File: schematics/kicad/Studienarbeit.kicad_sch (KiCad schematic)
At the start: 41 parts, among them J1 Barrel_Jack_Switch, U1 ESP32-WROOM-32E, U2 PCM5102, U3 MCP6001-OT, U4 MCP6001-OT, U5 MCP6001, U6 TPA711

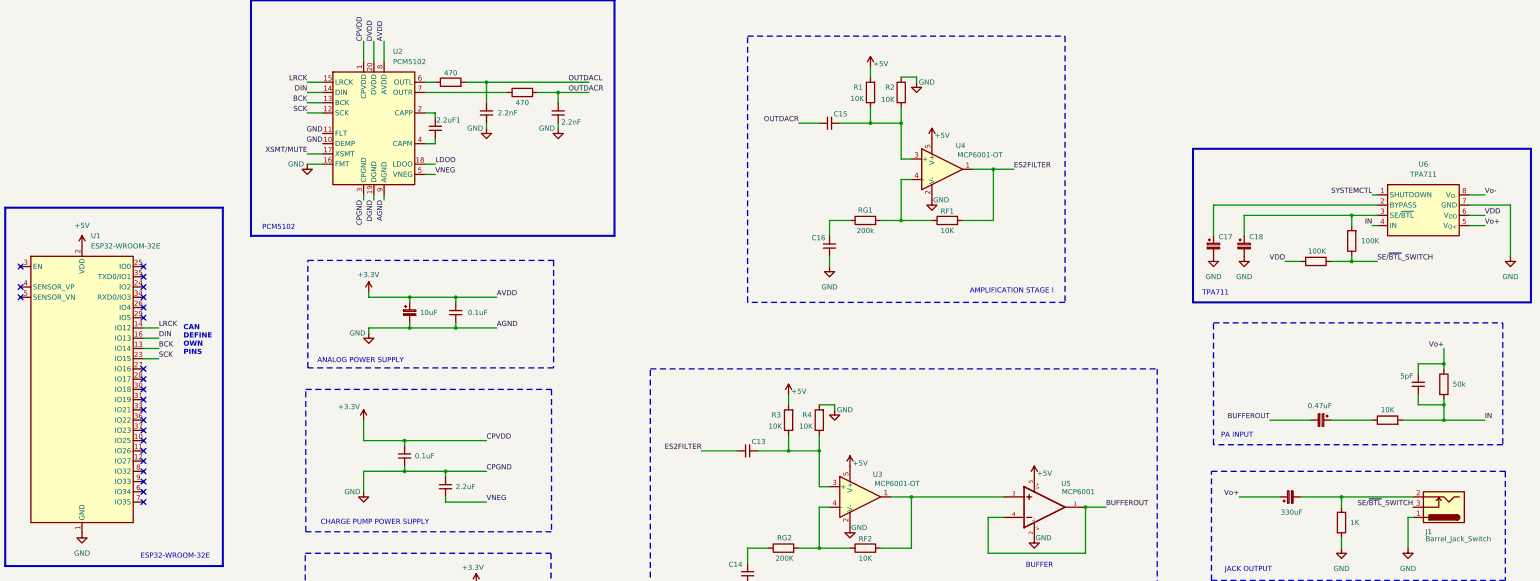
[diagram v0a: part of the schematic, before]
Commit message: KiCad: Fixed a few ERC errors.
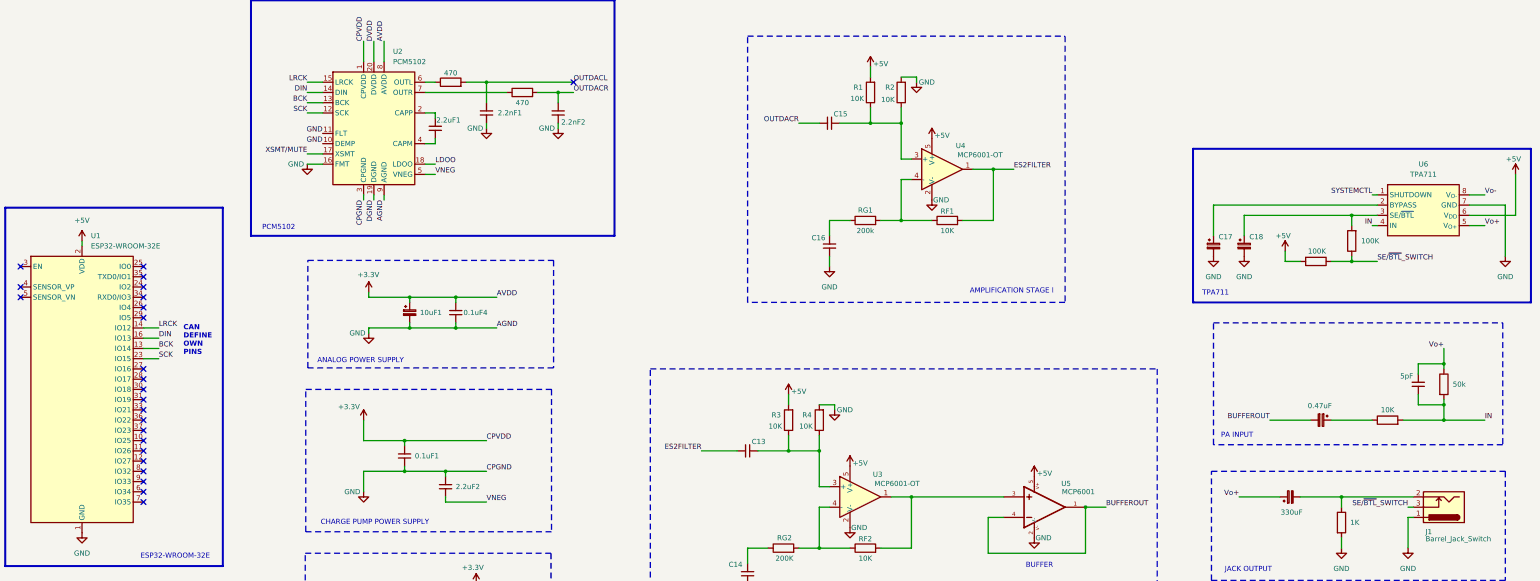
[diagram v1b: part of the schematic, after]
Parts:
- renumbered 0.1uF to 0.1uF1, 0.1uF to 0.1uF4, 10uF to 10uF1, 2.2nF to 2.2nF1, 2.2nF to 2.2nF2, 2.2uF to 2.2uF2, ROUTDACL to ROUTDACL1, ROUTDACR to ROUTDACR1
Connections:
- net VDD is gone; now on net +5V: R12.2, U6.6 (V_{DD})
- no-connect marks 23 -> 24

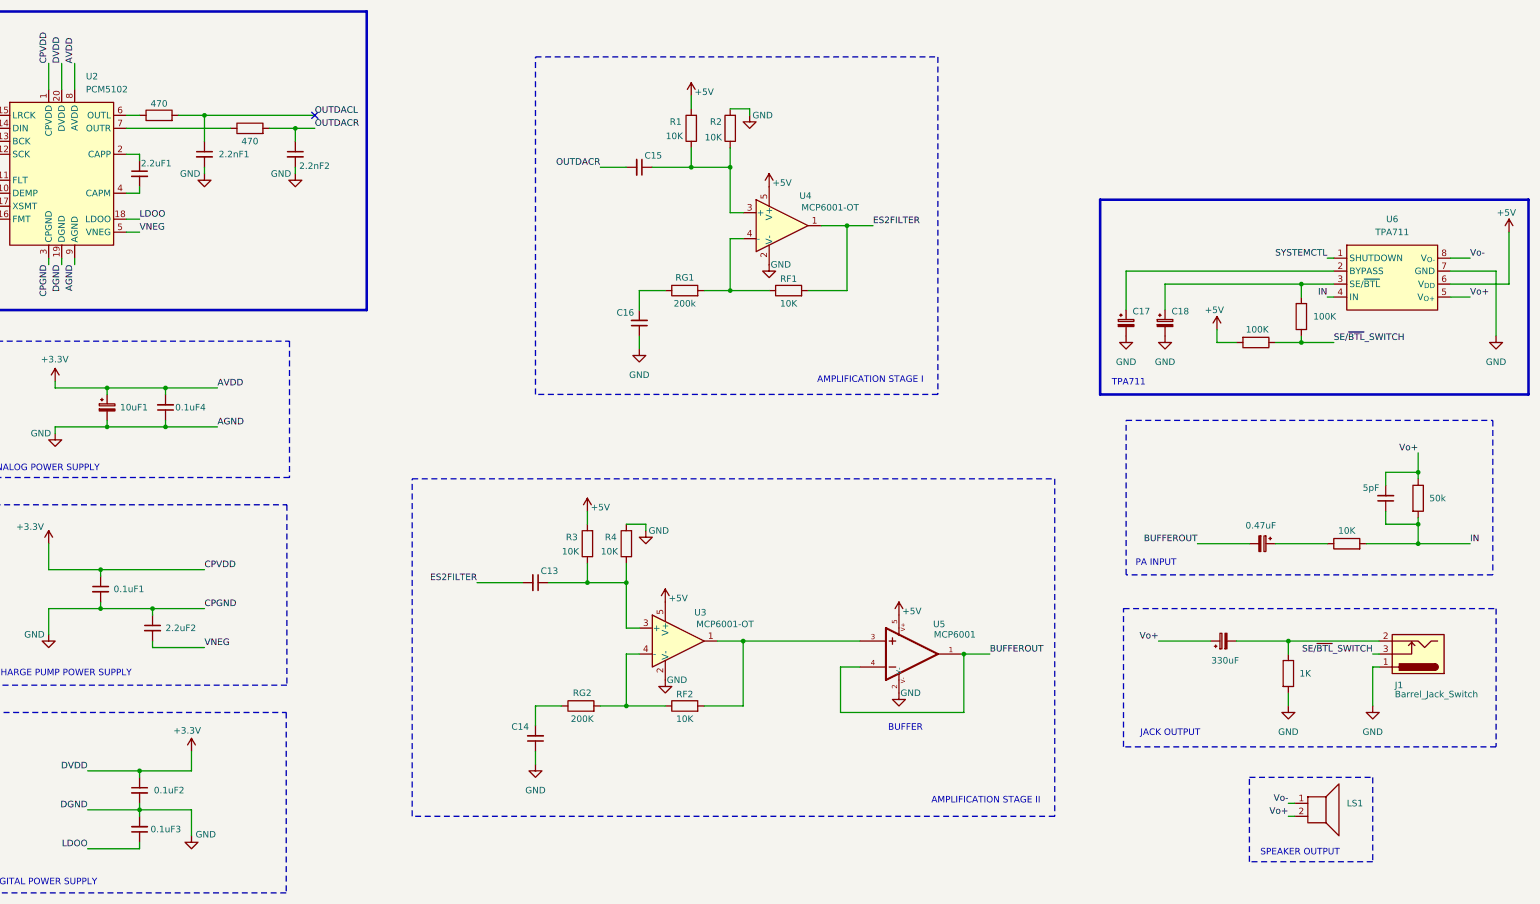
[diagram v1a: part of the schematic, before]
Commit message: KiCad: Dimentioned Cs.
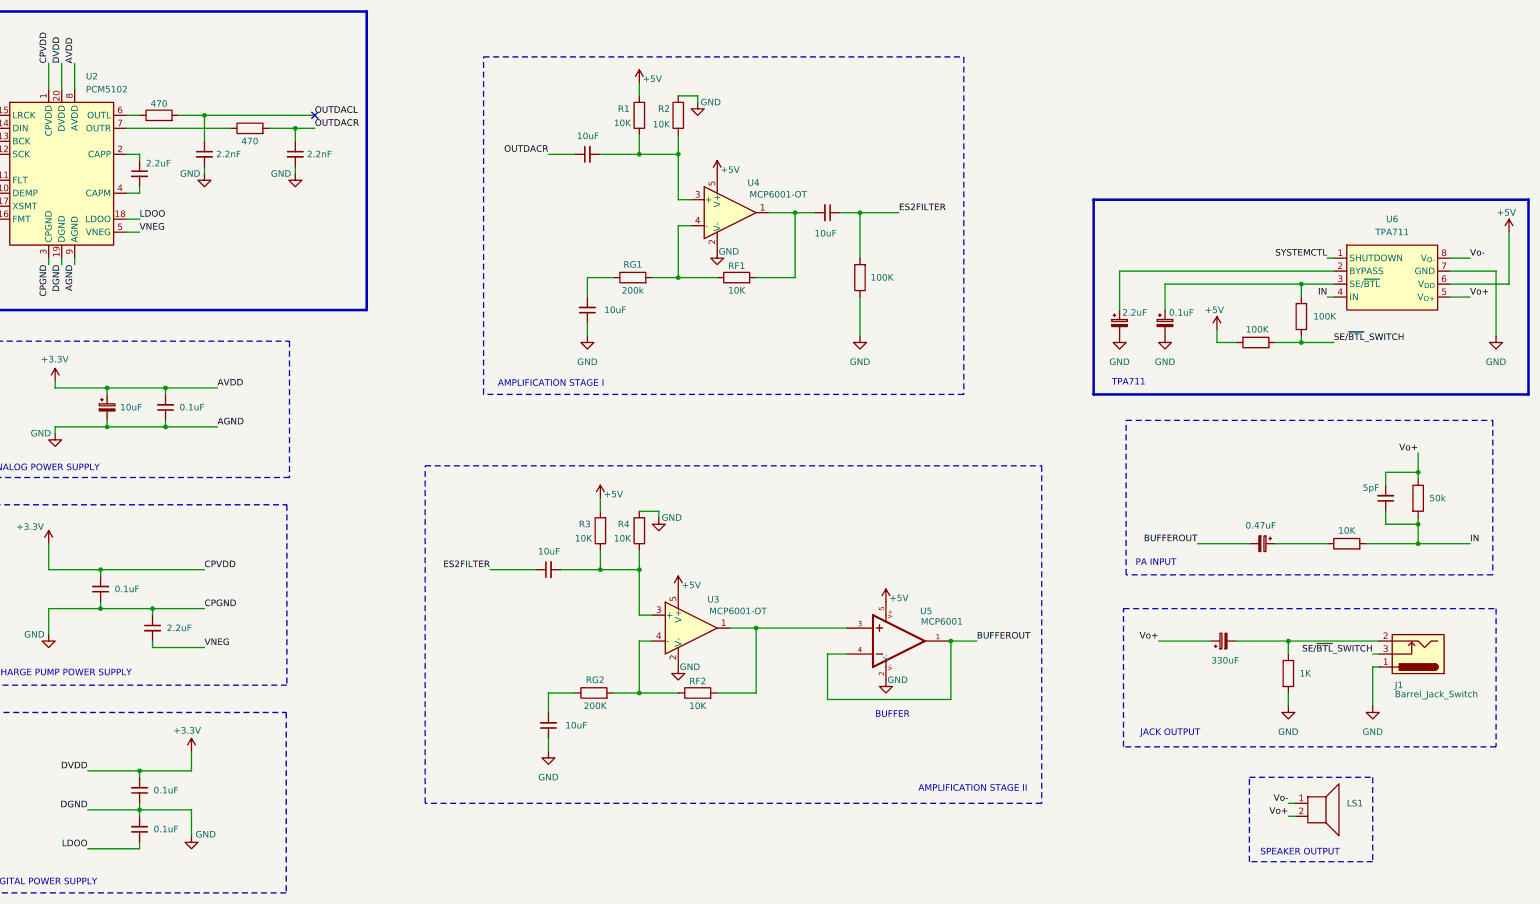
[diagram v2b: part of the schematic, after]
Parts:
- removed 0.1uF1, 0.1uF2, 0.1uF3, 2.2nF1, 2.2nF2, 2.2uF2, C13, C14, C15: C_Small, symbol Device:C_Small
- added C1_CPPS_PCM, C1_DPS_PCM, C2_DPS_PCM: 0.1uF, Capacitor_SMD:C_1206_3216Metric_Pad1.33x1.80mm_HandSolder, symbol Device:C_Small
- added C2_CPPS_PCM: 2.2uF, Capacitor_SMD:C_0805_2012Metric_Pad1.18x1.45mm_HandSolder, symbol Device:C_Small
- added CG1_PCM5102, CG2_PCM5102: 2.2nF, Capacitor_SMD:C_1206_3216Metric_Pad1.33x1.80mm_HandSolder, symbol Device:C_Small
- added C_COUPLING_AMPSTAGE1, C_GND_AMPSTAGE, C_GND_AMPSTAGE?, C_IN_AMPSTAGE: 10uF, Capacitor_SMD:C_1206_3216Metric_Pad1.33x1.80mm_HandSolder, symbol Device:C_Small
- added R_COUPLING_AMPSTAGE1: 100K, LED_SMD:LED_0805_2012Metric_Pad1.15x1.40mm_HandSolder, symbol Device:R
- C1_APS_PCM5102: renamed from 10uF1; value C_Polarized_Small -> 10uF; footprint (none) -> Capacitor_SMD:C_1206_3216Metric_Pad1.33x1.80mm_HandSolder
- C2_APS_PCM5102: renamed from 0.1uF4; value C_Small -> 0.1uF; footprint (none) -> Capacitor_SMD:C_1206_3216Metric_Pad1.33x1.80mm_HandSolder
- CA_PCM5102: renamed from 2.2uF1; value C_Small -> 2.2uF; footprint (none) -> Capacitor_SMD:C_0805_2012Metric_Pad1.18x1.45mm_HandSolder
- CB_TPA: renamed from C17; value C_Polarized_Small -> 2.2uF; footprint (none) -> Capacitor_SMD:C_0805_2012Metric_Pad1.18x1.45mm_HandSolder
- CC_TPA711, CF_TPA711, CI_TPA711: footprint (none) -> Capacitor_SMD:C_1206_3216Metric_Pad1.33x1.80mm_HandSolder
- C_GND_AMPSTAGE1: renamed from C16; footprint (none) -> Capacitor_SMD:C_1206_3216Metric_Pad1.33x1.80mm_HandSolder
- C_SE/BTL_TPA: renamed from C18; value C_Polarized_Small -> 0.1uF; footprint (none) -> Capacitor_SMD:C_1206_3216Metric_Pad1.33x1.80mm_HandSolder
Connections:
- net +3.3V: now also C1_CPPS_PCM.2, C1_DPS_PCM.2
- net ES2FILTER: now also C_COUPLING_AMPSTAGE1.1, C_IN_AMPSTAGE.1, R_COUPLING_AMPSTAGE1.2; no longer RF1.2, U4.1
- net GND: now also C1_CPPS_PCM.1, C1_DPS_PCM.1, C2_CPPS_PCM.1, C2_DPS_PCM.2, CG1_PCM5102.2, CG2_PCM5102.2, C_GND_AMPSTAGE.1, R_COUPLING_AMPSTAGE1.1
- net LDOO: now also C2_DPS_PCM.1
- net OUTDACL: now also CG1_PCM5102.1
- net OUTDACR: now also CG2_PCM5102.1, C_GND_AMPSTAGE?.1
- net VNEG: now also C2_CPPS_PCM.2
- net at R3.1, R4.1, U3.3 (+): now also C_IN_AMPSTAGE.2
- net at R1.1, R2.1, U4.3 (+): now also C_GND_AMPSTAGE?.2
- net at RG2.1: now also C_GND_AMPSTAGE.2
- new net: C_COUPLING_AMPSTAGE1.2, RF1.2, U4.1
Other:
- moved on the sheet: R1, R2, R3, R4, RF1, RF2, RG1, RG2, U3, U4, U5

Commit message: Added footprint folder for imported footprints.
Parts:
- U3, U4: footprint Package_TO_SOT_SMD:SOT-23-5 -> MCP6001_SOT23-5:SOT23-5
- gave numbers to parts that had none: 1
- renumbered C1_CPPS_PCM to C1_CPPS_PCM1, C1_DPS_PCM to C1_DPS_PCM1, C2_CPPS_PCM to C2_CPPS_PCM1, C2_DPS_PCM to C2_DPS_PCM1, CB_TPA to CB_TPA1, C_GND_AMPSTAGE to C_GND_AMPSTAGE2, C_IN_AMPSTAGE to C_IN_AMPSTAGE1, C_SE/BTL_TPA to C_SE/BTL_TPA1
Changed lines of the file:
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@@
 		(on_board yes)
 		(dnp no)
-		(property "Reference" "C_SE/BTL_TPA"
+		(property "Reference" "C_SE/BTL_TPA1"
 			(at 330.2 128.524 0)
 			(effects
@@
 			(project "Studienarbeit"
 				(path "/e1f471d3-f850-4433-b54a-c7e6f7857097"
-					(reference "C_SE/BTL_TPA")
+					(reference "C_SE/BTL_TPA1")
 					(unit 1)
 				)
@@
 		(on_board yes)
 		(dnp no)
-		(property "Reference" "C_GND_AMPSTAGE"
+		(property "Reference" "C_GND_AMPSTAGE2"
 			(at 207.264 207.518 0)
 			(effects
@@
 			(project "Studienarbeit"
 				(path "/e1f471d3-f850-4433-b54a-c7e6f7857097"
-					(reference "C_GND_AMPSTAGE")
+					(reference "C_GND_AMPSTAGE2")
 					(unit 1)
 				)
@@
 			)
 		)
-		(property "Footprint" "Package_TO_SOT_SMD:SOT-23-5"
+		(property "Footprint" "MCP6001_SOT23-5:SOT23-5"
 			(at 241.3 114.3 0)
 			(effects
@@
 		(on_board yes)
 		(dnp no)
-		(property "Reference" "C2_CPPS_PCM"
+		(property "Reference" "C2_CPPS_PCM1"
 			(at 131.064 188.468 0)
 			(effects
@@
 			(project "Studienarbeit"
 				(path "/e1f471d3-f850-4433-b54a-c7e6f7857097"
-					(reference "C2_CPPS_PCM")
+					(reference "C2_CPPS_PCM1")
 					(unit 1)
 				)
@@
 			)
 		)
-		(property "Footprint" "Package_TO_SOT_SMD:SOT-23-5"
+		(property "Footprint" "MCP6001_SOT23-5:SOT23-5"
 			(at 233.68 195.58 0)
 			(effects
@@
 		(on_board yes)
 		(dnp no)
-		(property "Reference" "C1_CPPS_PCM"
+		(property "Reference" "C1_CPPS_PCM1"
 			(at 129.794 182.88 0)
 			(effects
@@
 			(project "Studienarbeit"
 				(path "/e1f471d3-f850-4433-b54a-c7e6f7857097"
-					(reference "C1_CPPS_PCM")
+					(reference "C1_CPPS_PCM1")
 					(unit 1)
 				)
@@
 		(on_board yes)
 		(dnp no)
-		(property "Reference" "C_GND_AMPSTAGE?"
+		(property "Reference" "C_GND_AMPSTAGE3"
 			(at 217.932 96.774 0)
 			(effects
@@
 			(project "Studienarbeit"
 				(path "/e1f471d3-f850-4433-b54a-c7e6f7857097"
-					(reference "C_GND_AMPSTAGE?")
+					(reference "C_GND_AMPSTAGE3")
 					(unit 1)
 				)
@@
 		(on_board yes)
 		(dnp no)
-		(property "Reference" "C_IN_AMPSTAGE"
+		(property "Reference" "C_IN_AMPSTAGE1"
 			(at 210.312 178.054 0)
 			(effects
@@
 			(project "Studienarbeit"
 				(path "/e1f471d3-f850-4433-b54a-c7e6f7857097"
-					(reference "C_IN_AMPSTAGE")
+					(reference "C_IN_AMPSTAGE1")
 					(unit 1)
 				)
@@
 		(on_board yes)
 		(dnp no)
-		(property "Reference" "C2_DPS_PCM"
+		(property "Reference" "C2_DPS_PCM1"
 			(at 137.414 229.87 0)
 			(effects
@@
 			(project "Studienarbeit"
 				(path "/e1f471d3-f850-4433-b54a-c7e6f7857097"
-					(reference "C2_DPS_PCM")
+					(reference "C2_DPS_PCM1")
 					(unit 1)
 				)
@@
 		(on_board yes)
 		(dnp no)
-		(property "Reference" "C1_DPS_PCM"
+		(property "Reference" "C1_DPS_PCM1"
 			(at 137.414 222.25 0)
 			(effects
@@
 			(project "Studienarbeit"
 				(path "/e1f471d3-f850-4433-b54a-c7e6f7857097"
-					(reference "C1_DPS_PCM")
+					(reference "C1_DPS_PCM1")
 					(unit 1)
 				)
@@
 		(on_board yes)
 		(dnp no)
-		(property "Reference" "CB_TPA"
+		(property "Reference" "CB_TPA1"
 			(at 321.31 128.524 0)
 			(effects
@@
 			(project "Studienarbeit"
 				(path "/e1f471d3-f850-4433-b54a-c7e6f7857097"
-					(reference "CB_TPA")
+					(reference "CB_TPA1")
 					(unit 1)
 				)

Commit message: Added ESP32 Footprint.
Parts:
- U3, U4: footprint MCP6001_SOT23-5:SOT23-5 -> Package_TO_SOT_SMD:SOT-23-5
- U5: footprint MCP6001:SOT23-5 -> Package_TO_SOT_SMD:SOT-23-5
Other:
- moved on the sheet: J1, LS1

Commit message: KiCad: Draft of PCB.
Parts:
- U1: footprint RF_Module:ESP32-WROOM-32D -> RF_Module:ESP32-WROOM-32E
- U6: footprint Package_DFN_QFN:Texas_DRB0008A -> Package_SO:Texas_DGN0008D_VSSOP-8-1EP_3x3mm_P0.65mm_EP2x2.94mm_Mask1.57x1.89mm
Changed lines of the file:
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@@
 	(text "AMPLIFICATION STAGE I"
 		(exclude_from_sim no)
-		(at 208.788 142.748 0)
+		(at 208.28 142.24 0)
 		(effects
 			(font
@@
 			)
 		)
-		(property "Footprint" "RF_Module:ESP32-WROOM-32D"
+		(property "Footprint" "RF_Module:ESP32-WROOM-32E"
 			(at 57.15 200.66 0)
 			(effects
@@
 			)
 		)
-		(property "Footprint" "Package_DFN_QFN:Texas_DRB0008A"
+		(property "Footprint" "Package_SO:Texas_DGN0008D_VSSOP-8-1EP_3x3mm_P0.65mm_EP2x2.94mm_Mask1.57x1.89mm"
 			(at 373.38 121.92 0)
 			(effects

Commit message: KiCad: Added test points in the schematic.
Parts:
- added C_INPUT_LDO1: 0.47uF, Capacitor_SMD:C_1206_3216Metric_Pad1.33x1.80mm_HandSolder, symbol Device:C_Small
- added C_OUTPUT_LDO1: 22uF, Capacitor_SMD:C_1206_3216Metric_Pad1.33x1.80mm_HandSolder, symbol Device:C_Small
- added TP_AVDD_PCM, TP_BCK, TP_CPVDD_PCM, TP_DIN, TP_DVDD_PCM, TP_GND_ESP32, TP_INPUTBIAS_AS1, TP_INPUTBIAS_AS2, TP_LM2940_+5V, TP_LRCK, TP_OUTPUT_AS1, TP_OUTPUT_AS2, TP_OUTPUT_BUFFER, TP_VCC_AS1, TP_VCC_AS2, TP_VCC_Buffer, TP_VDD_TPA, TP_Vo+_TPA, TP_Vo-_TPA: TestPoint, symbol Connector:TestPoint
- added U7: LM2940CT-5.0, Package_TO_SOT_THT:TO-220-3_Horizontal_TabDown, symbol LM2940-5.0:LM2940CT-5.0
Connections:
- net +3.3V: now also TP_AVDD_PCM.1, TP_CPVDD_PCM.1, TP_DVDD_PCM.1
- net +5V: now also C_OUTPUT_LDO1.2, TP_LM2940_+5V.1, TP_VCC_AS1.1, TP_VCC_AS2.1, TP_VCC_Buffer.1, TP_VDD_TPA.1, U7.3 (OUT)
- net BCK: now also TP_BCK.1
- net BUFFEROUT: now also TP_OUTPUT_BUFFER.1
- net DIN: now also TP_DIN.1
- net ES2FILTER: now also TP_OUTPUT_AS1.1
- net GND: now also C_INPUT_LDO1.1, C_OUTPUT_LDO1.1, TP_GND_ESP32.1, U7.2 (GND)
- net LRCK: now also TP_LRCK.1
- net SCK: no longer U1.23 (IO15)
- net Vo+: now also TP_Vo+_TPA.1
- net Vo-: now also TP_Vo-_TPA.1
- net at RF2.2, U3.1, U5.3: now also TP_OUTPUT_AS2.1
- net at C_GND_AMPSTAGE3.2, R1.1, R2.1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: now also TP_INPUTBIAS_AS1.1
- net at C_IN_AMPSTAGE1.2, R3.1, R4.1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: now also TP_INPUTBIAS_AS2.1
- new net +15V: C_INPUT_LDO1.2, U7.1 (IN)
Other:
- note added: "LM2940CT"
- moved on the sheet: J1, LS1, R1, R2, R3, R4, RF1, RF2, RG1, RG2, U1, U2
